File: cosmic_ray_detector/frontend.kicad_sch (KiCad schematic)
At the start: 15 parts

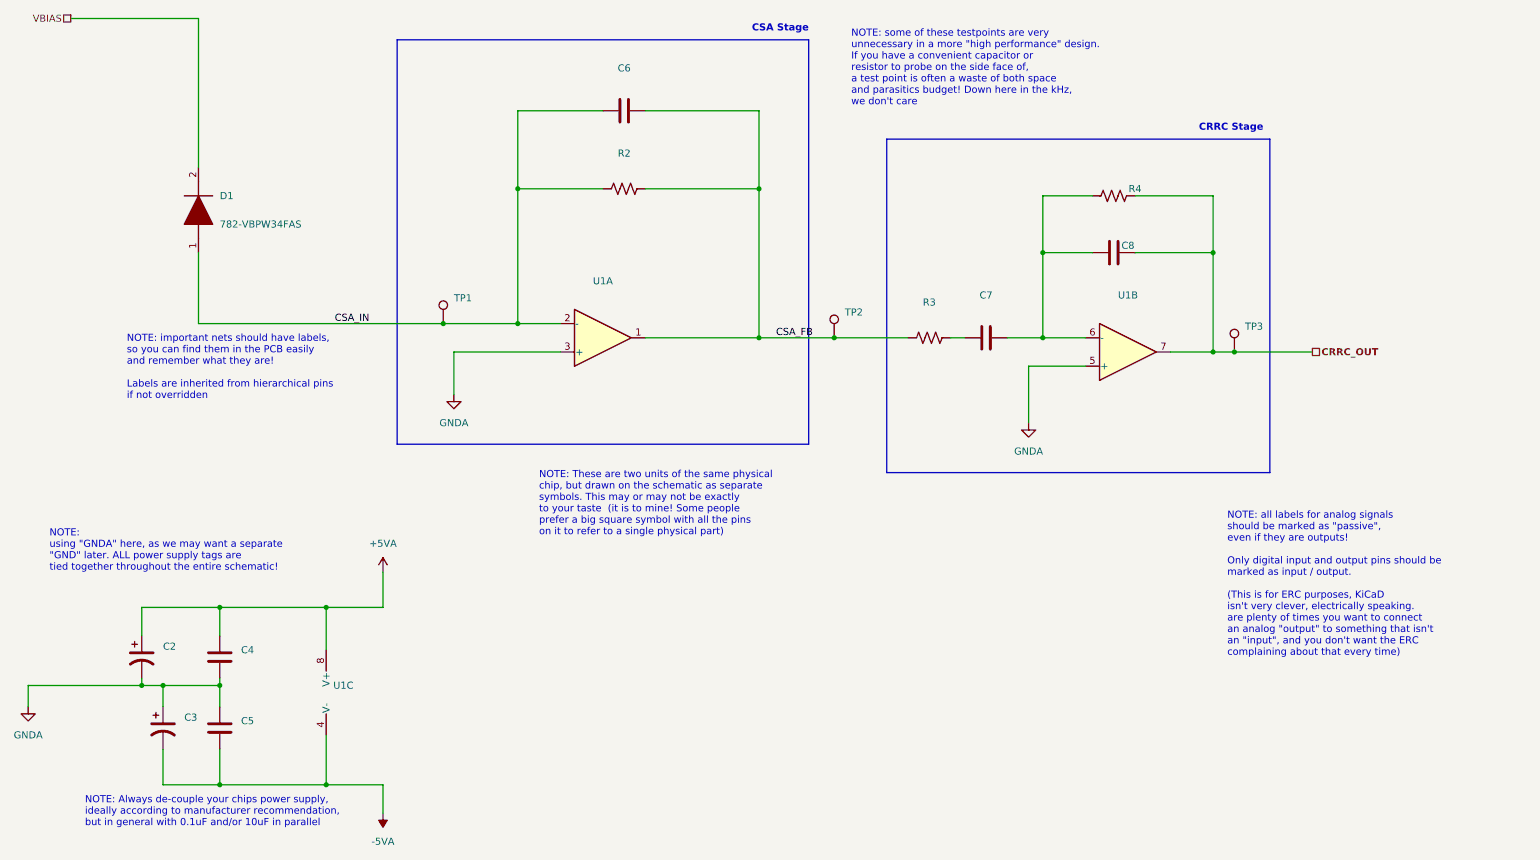
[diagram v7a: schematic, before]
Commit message: add conceptual design, tweaks to schematics
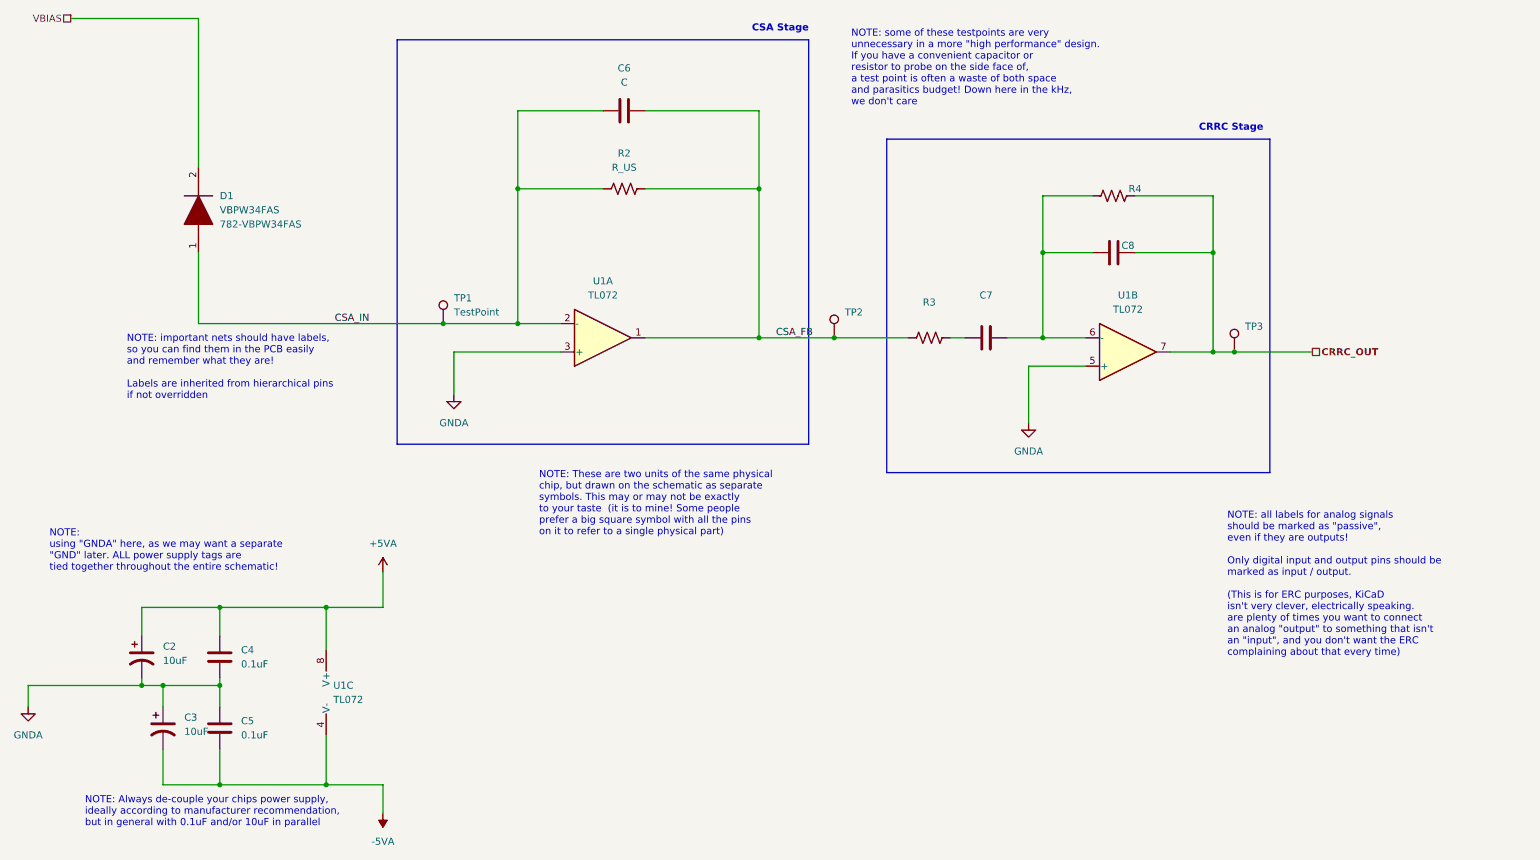
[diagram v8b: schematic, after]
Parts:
- C2, C3: value (none) -> 10uF; footprint (none) -> cosmic_ray_detector_lib:MAL215375109E3
- C4, C5: value (none) -> 0.1uF; footprint (none) -> Capacitor_SMD:C_0402_1005Metric
- C6: value (none) -> C; footprint (none) -> Capacitor_SMD:C_0402_1005Metric
- C7, C8: value (none) -> ~; footprint (none) -> Capacitor_SMD:C_0402_1005Metric
- D1: value (none) -> VBPW34FAS; footprint (none) -> cosmic_ray_detector_lib:VBPW34FAS
- R2: value (none) -> R_US; footprint (none) -> Resistor_SMD:R_0402_1005Metric
- R3, R4: value (none) -> ~; footprint (none) -> Resistor_SMD:R_0402_1005Metric
- TP1: value (none) -> TestPoint; footprint (none) -> cosmic_ray_detector_lib:harwin_tp_SMD
- TP2, TP3: value (none) -> ~; footprint (none) -> cosmic_ray_detector_lib:harwin_tp_SMD
- U1: value (none) -> TL072; footprint (none) -> Package_SO:SO-8_3.9x4.9mm_P1.27mm
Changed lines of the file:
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@@
     (in_bom yes) (on_board yes) (fields_autoplaced)
     (property "Reference" "U1" (id 0) (at 219.71 97.79 0))
-    (property "Value" "" (id 1) (at 219.71 100.33 0))
-    (property "Footprint" "" (id 2) (at 219.71 107.95 0)
+    (property "Value" "TL072" (id 1) (at 219.71 100.33 0))
+    (property "Footprint" "Package_SO:SO-8_3.9x4.9mm_P1.27mm" (id 2) (at 219.71 107.95 0)
       (effects (font (size 1.27 1.27)) hide)
     )
@@
     (in_bom yes) (on_board yes)
     (property "Reference" "R4" (id 0) (at 220.98 78.74 90))
-    (property "Value" "" (id 1) (at 217.17 76.2 90))
-    (property "Footprint" "" (id 2) (at 217.424 78.994 90)
+    (property "Value" "~" (id 1) (at 217.17 76.2 90))
+    (property "Footprint" "Resistor_SMD:R_0402_1005Metric" (id 2) (at 217.424 78.994 90)
       (effects (font (size 1.27 1.27)) hide)
     )
@@
     (in_bom yes) (on_board yes) (fields_autoplaced)
     (property "Reference" "C7" (id 0) (at 194.31 97.79 90))
-    (property "Value" "" (id 1) (at 194.31 100.33 90))
-    (property "Footprint" "" (id 2) (at 198.12 104.4448 0)
+    (property "Value" "~" (id 1) (at 194.31 100.33 90))
+    (property "Footprint" "Capacitor_SMD:C_0402_1005Metric" (id 2) (at 198.12 104.4448 0)
       (effects (font (size 1.27 1.27)) hide)
     )
@@
     (in_bom yes) (on_board yes) (fields_autoplaced)
     (property "Reference" "R2" (id 0) (at 129.54 72.39 90))
-    (property "Value" "" (id 1) (at 129.54 74.93 90))
-    (property "Footprint" "" (id 2) (at 129.794 77.724 90)
+    (property "Value" "R_US" (id 1) (at 129.54 74.93 90))
+    (property "Footprint" "Resistor_SMD:R_0402_1005Metric" (id 2) (at 129.794 77.724 90)
       (effects (font (size 1.27 1.27)) hide)
     )
@@
       (effects (font (size 1.27 1.27)) (justify left))
     )
-    (property "Value" "" (id 1) (at 57.15 82.5499 90)
-      (effects (font (size 1.27 1.27)) (justify left))
-    )
-    (property "Footprint" "" (id 2) (at 53.34 86.36 0)
+    (property "Value" "VBPW34FAS" (id 1) (at 57.15 82.5499 90)
+      (effects (font (size 1.27 1.27)) (justify left))
+    )
+    (property "Footprint" "cosmic_ray_detector_lib:VBPW34FAS" (id 2) (at 53.34 86.36 0)
       (effects (font (size 1.27 1.27)) (justify left) hide)
     )
@@
       (effects (font (size 1.27 1.27)) (justify left))
     )
-    (property "Value" "" (id 1) (at 60.96 163.8299 0)
-      (effects (font (size 1.27 1.27)) (justify left))
-    )
-    (property "Footprint" "" (id 2) (at 58.1152 166.37 0)
+    (property "Value" "0.1uF" (id 1) (at 60.96 163.8299 0)
+      (effects (font (size 1.27 1.27)) (justify left))
+    )
+    (property "Footprint" "Capacitor_SMD:C_0402_1005Metric" (id 2) (at 58.1152 166.37 0)
       (effects (font (size 1.27 1.27)) hide)
     )
@@
       (effects (font (size 1.27 1.27)) (justify left))
     )
-    (property "Value" "" (id 1) (at 50.8 175.8949 0)
-      (effects (font (size 1.27 1.27)) (justify left))
-    )
-    (property "Footprint" "" (id 2) (at 46.99 175.26 0)
+    (property "Value" "10uF" (id 1) (at 50.8 175.8949 0)
+      (effects (font (size 1.27 1.27)) (justify left))
+    )
+    (property "Footprint" "cosmic_ray_detector_lib:MAL215375109E3" (id 2) (at 46.99 175.26 0)
       (effects (font (size 1.27 1.27)) hide)
     )
@@
     (in_bom yes) (on_board yes) (fields_autoplaced)
     (property "Reference" "R3" (id 0) (at 184.15 99.06 90))
-    (property "Value" "" (id 1) (at 184.15 101.6 90))
-    (property "Footprint" "" (id 2) (at 184.404 104.394 90)
+    (property "Value" "~" (id 1) (at 184.15 101.6 90))
+    (property "Footprint" "Resistor_SMD:R_0402_1005Metric" (id 2) (at 184.404 104.394 90)
       (effects (font (size 1.27 1.27)) hide)
     )
@@
     (in_bom yes) (on_board yes)
     (property "Reference" "C8" (id 0) (at 219.71 88.9 90))
-    (property "Value" "" (id 1) (at 217.17 85.09 90))
-    (property "Footprint" "" (id 2) (at 220.98 89.2048 0)
+    (property "Value" "~" (id 1) (at 217.17 85.09 90))
+    (property "Footprint" "Capacitor_SMD:C_0402_1005Metric" (id 2) (at 220.98 89.2048 0)
       (effects (font (size 1.27 1.27)) hide)
     )
@@
       (effects (font (size 1.27 1.27)) (justify left))
     )
-    (property "Value" "" (id 1) (at 46.99 163.1949 0)
-      (effects (font (size 1.27 1.27)) (justify left))
-    )
-    (property "Footprint" "" (id 2) (at 43.18 162.56 0)
+    (property "Value" "10uF" (id 1) (at 46.99 163.1949 0)
+      (effects (font (size 1.27 1.27)) (justify left))
+    )
+    (property "Footprint" "cosmic_ray_detector_lib:MAL215375109E3" (id 2) (at 43.18 162.56 0)
       (effects (font (size 1.27 1.27)) hide)
     )
@@
     (in_bom yes) (on_board yes) (fields_autoplaced)
     (property "Reference" "C6" (id 0) (at 129.54 57.15 90))
-    (property "Value" "" (id 1) (at 129.54 59.69 90))
-    (property "Footprint" "" (id 2) (at 133.35 63.8048 0)
+    (property "Value" "C" (id 1) (at 129.54 59.69 90))
+    (property "Footprint" "Capacitor_SMD:C_0402_1005Metric" (id 2) (at 133.35 63.8048 0)
       (effects (font (size 1.27 1.27)) hide)
     )
@@
       (effects (font (size 1.27 1.27)) (justify left))
     )
-    (property "Value" "" (id 1) (at 99.06 100.8379 0)
-      (effects (font (size 1.27 1.27)) (justify left))
-    )
-    (property "Footprint" "" (id 2) (at 102.235 102.87 0)
+    (property "Value" "TestPoint" (id 1) (at 99.06 100.8379 0)
+      (effects (font (size 1.27 1.27)) (justify left))
+    )
+    (property "Footprint" "cosmic_ray_detector_lib:harwin_tp_SMD" (id 2) (at 102.235 102.87 0)
       (effects (font (size 1.27 1.27)) hide)
     )
@@
       (effects (font (size 1.27 1.27)) (justify left))
     )
-    (property "Value" "" (id 1) (at 60.96 176.5299 0)
-      (effects (font (size 1.27 1.27)) (justify left))
-    )
-    (property "Footprint" "" (id 2) (at 58.1152 179.07 0)
+    (property "Value" "0.1uF" (id 1) (at 60.96 176.5299 0)
+      (effects (font (size 1.27 1.27)) (justify left))
+    )
+    (property "Footprint" "Capacitor_SMD:C_0402_1005Metric" (id 2) (at 58.1152 179.07 0)
       (effects (font (size 1.27 1.27)) hide)
     )
@@
       (effects (font (size 1.27 1.27)) (justify left))
     )
-    (property "Value" "" (id 1) (at 169.037 103.3779 0)
-      (effects (font (size 1.27 1.27)) (justify left))
-    )
-    (property "Footprint" "" (id 2) (at 172.212 105.41 0)
+    (property "Value" "~" (id 1) (at 169.037 103.3779 0)
+      (effects (font (size 1.27 1.27)) (justify left))
+    )
+    (property "Footprint" "cosmic_ray_detector_lib:harwin_tp_SMD" (id 2) (at 172.212 105.41 0)
       (effects (font (size 1.27 1.27)) hide)
     )
@@
     (in_bom yes) (on_board yes) (fields_autoplaced)
     (property "Reference" "U1" (id 0) (at 125.73 95.25 0))
-    (property "Value" "" (id 1) (at 125.73 97.79 0))
-    (property "Footprint" "" (id 2) (at 125.73 105.41 0)
+    (property "Value" "TL072" (id 1) (at 125.73 97.79 0))
+    (property "Footprint" "Package_SO:SO-8_3.9x4.9mm_P1.27mm" (id 2) (at 125.73 105.41 0)
       (effects (font (size 1.27 1.27)) hide)
     )
@@
       (effects (font (size 1.27 1.27)) (justify left))
     )
-    (property "Value" "" (id 1) (at 77.47 170.1799 0)
-      (effects (font (size 1.27 1.27)) (justify left))
-    )
-    (property "Footprint" "" (id 2) (at 78.74 168.91 0)
+    (property "Value" "TL072" (id 1) (at 77.47 170.1799 0)
+      (effects (font (size 1.27 1.27)) (justify left))
+    )
+    (property "Footprint" "Package_SO:SO-8_3.9x4.9mm_P1.27mm" (id 2) (at 78.74 168.91 0)
       (effects (font (size 1.27 1.27)) hide)
     )
@@
       (effects (font (size 1.27 1.27)) (justify left))
     )
-    (property "Value" "" (id 1) (at 240.665 105.9179 0)
-      (effects (font (size 1.27 1.27)) (justify left))
-    )
-    (property "Footprint" "" (id 2) (at 243.84 107.95 0)
-      (effects (font (size 1.27 1.27)) hide)
-    )
+    (property "Value" "~" (id 1) (at 240.665 105.9179 0)
+      (effects (font (size 1.27 1.27)) (justify left))
+    )
+    (property "Footprint" "cosmic_ray_detector_lib:harwin_tp_SMD" (id 2) (at 243.84 107.95 0)
+      (effects (font (size 1.27 1.27)) hide)
+    )
